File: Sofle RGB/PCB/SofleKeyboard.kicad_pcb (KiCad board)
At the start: 2 copper layers, 137.2 x 109.2 mm, 95 parts, among them J1 LED, J2 4PIN, J3 OLED, J4 key leds, J5 backlight sel, J6 indicator bypass, P1 i2c_pin, P2 i2c_pin, SW1 SW_PUSH-MX_W_LED, SW10 SW_PUSH-MX_W_LED, SW11 SW_PUSH-MX_W_LED, SW12 SW_PUSH-MX_W_LED, SW13 SW_PUSH-MX_W_LED, SW14 SW_PUSH-MX_W_LED, SW15 SW_PUSH-MX_W_LED, SW16 SW_PUSH-MX_W_LED, SW17 SW_PUSH-MX_W_LED, SW18 SW_PUSH-MX_W_LED, SW19 SW_PUSH-MX_W_LED, SW2 SW_PUSH-MX_W_LED, SW20 SW_PUSH-MX_W_LED, SW21 SW_PUSH-MX_W_LED, SW22 SW_PUSH-MX_W_LED, SW23 SW_PUSH-MX_W_LED, SW24 SW_PUSH-MX_W_LED, SW25 Rotary_Encoder_Switch, SW26 SW_PUSH-MX_W_LED, SW27 SW_PUSH-MX_W_LED, SW28 SW_PUSH-MX_W_LED, SW29 SW_PUSH-MX_W_LED, SW3 SW_PUSH-MX_W_LED, SW30 SW_PUSH-MX_W_LED, SW4 SW_PUSH-MX_W_LED, SW5 SW_PUSH-MX_W_LED, SW6 SW_PUSH-MX_W_LED, SW7 SW_PUSH-MX_W_LED, SW8 SW_PUSH-MX_W_LED, SW9 SW_PUSH-MX_W_LED, U1 ProMicro

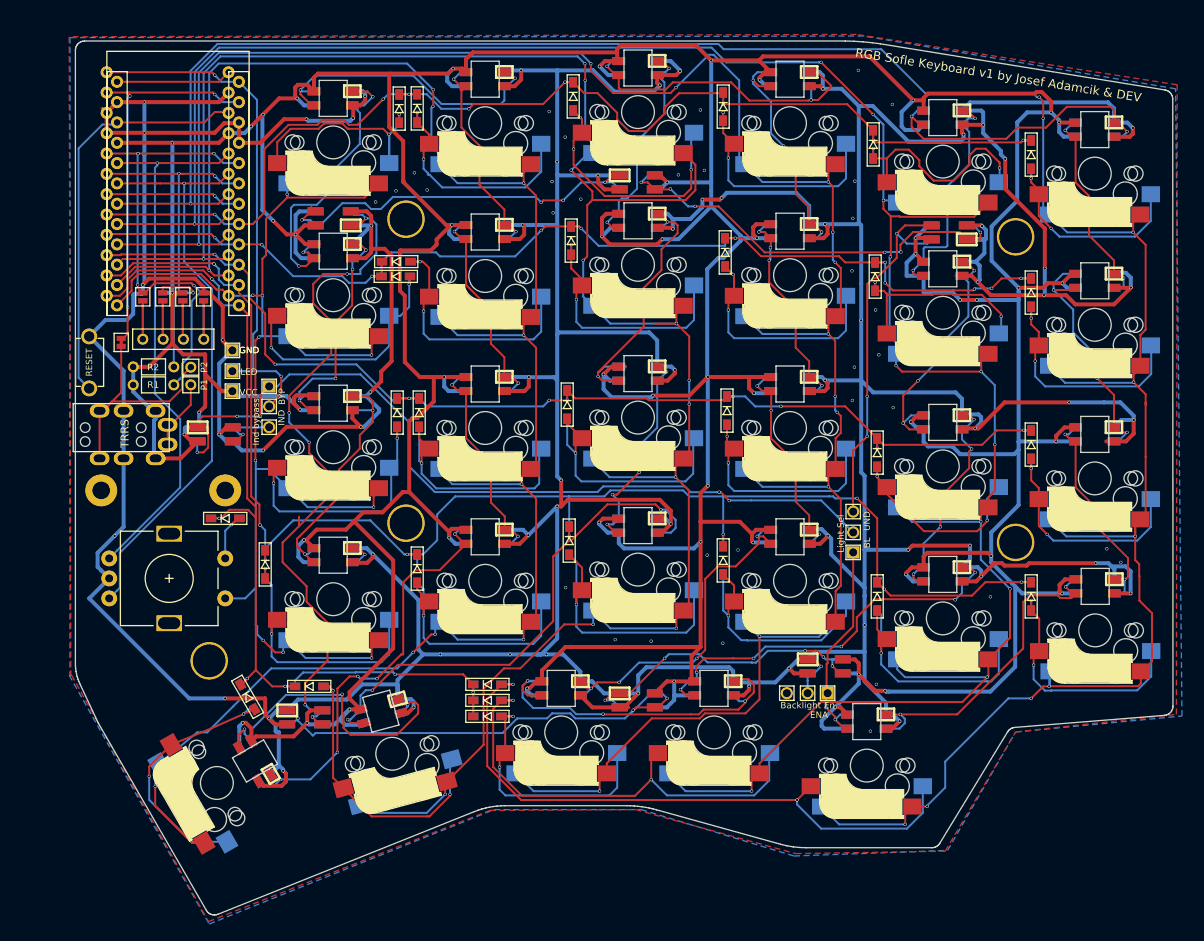
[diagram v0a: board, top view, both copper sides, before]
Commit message: added placement changes from r2, routed need to make any other changes, do pcb plates, and fix up the folders for mergeing
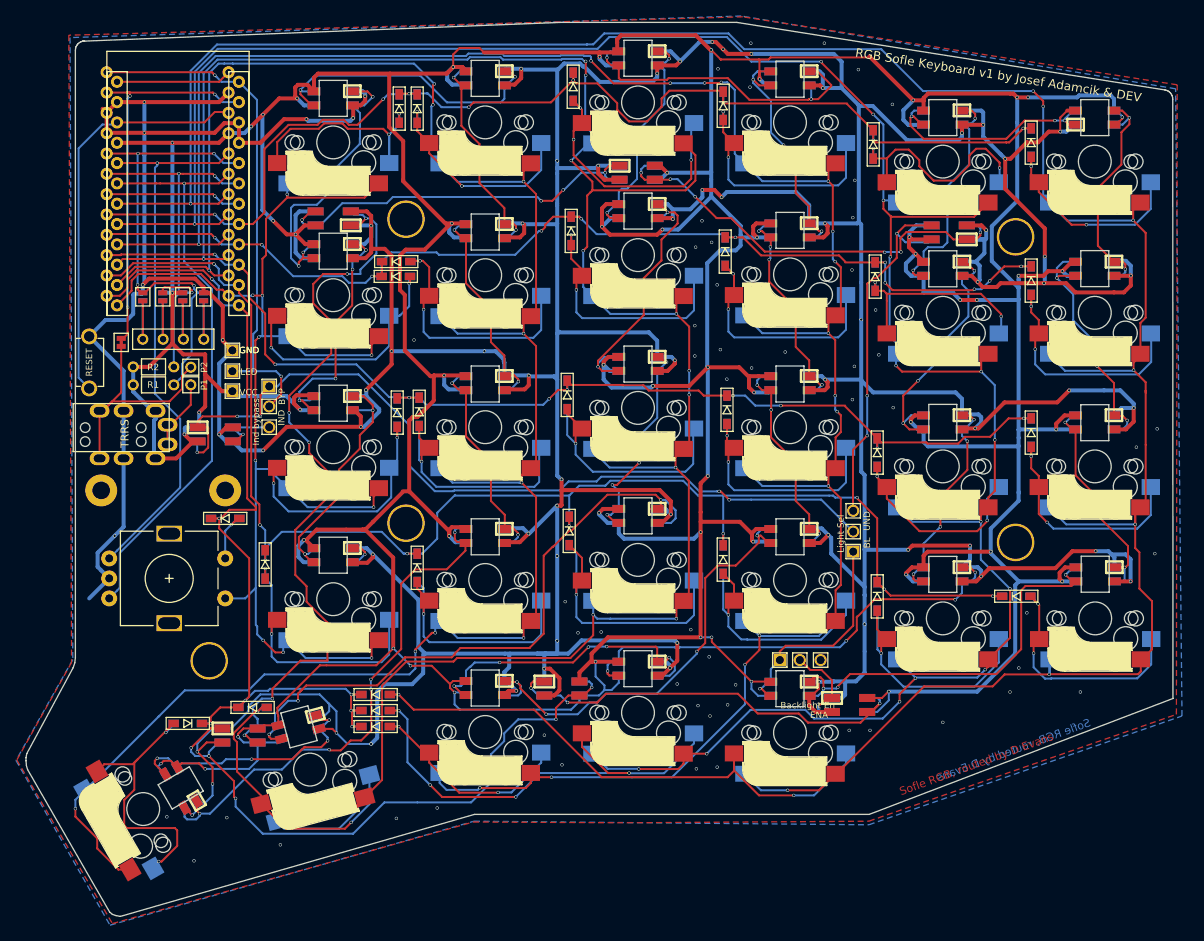
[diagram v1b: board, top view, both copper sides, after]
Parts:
- SW6: moved to B.Cu
- moved D28 14.0 mm to (125.8, 123.0)
- moved D29 14.0 mm to (125.8, 121.0)
- moved D30 14.0 mm to (125.8, 119.0)
- moved SW27 10.5 mm to (117.6, 128.4)
- moved SW30 10.4 mm to (177.6, 123.8)
- moved SW26 9.83 mm to (96.7, 133.4)
- moved SW29 9.81 mm to (158.6, 121.3)
- moved D35 9.53 mm to (149.1, 118.3)
- moved SW28 9.50 mm to (139.5, 123.7)
- moved D34 8.41 mm to (108.8, 124.1)
- moved D26 8.18 mm to (102.3, 122.6), turned to 180 degrees
- moved D27 7.55 mm to (110.4, 120.6)
- moved J5 7.27 mm to (176.3, 114.7), turned to 90 degrees
- moved D36 5.70 mm to (185.1, 120.3)
- moved D24 1.87 mm to (205.9, 106.7), turned to 0 degrees
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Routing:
- net VCC: track 911.1 -> 938.6 mm, vias 52 -> 56
- net Net-(D34-Pad1): track 59.0 -> 77.3 mm, vias 3 -> 5
- net Net-(SW22-Pad3): track 42.2 -> 56.5 mm
- net Net-(D35-Pad1): track 40.1 -> 53.7 mm, vias 5 -> 3
- net col4: track 245.1 -> 258.7 mm
- net Net-(SW21-Pad1): track 66.6 -> 79.9 mm
- net Net-(SW20-Pad3): track 53.9 -> 66.2 mm
- net col3: track 267.0 -> 276.7 mm
- net Net-(SW28-Pad3): track 47.7 -> 38.0 mm, vias 3 -> 5
- net Net-(SW24-Pad3): track 41.0 -> 50.3 mm, vias 2 -> 3
- net Net-(SW5-Pad3): track 39.6 -> 31.1 mm, vias 2 -> 3
- net Net-(SW26-Pad3): track 39.6 -> 31.5 mm, vias 3 -> 4
- net row3: track 191.0 -> 183.2 mm
- net Net-(SW23-Pad1): track 51.1 -> 58.4 mm, vias 6 -> 4
- net Net-(D30-Pad2): track 78.4 -> 71.2 mm
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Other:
- board size 137.2 x 109.2 mm -> 143.4 x 111.8 mm
- board text added: "Sofle RGB, routed by D Evans"

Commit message: release version of the sofle rgb, routing done, case made, there are some slight oddities in the spacing of some keys, but they are very small
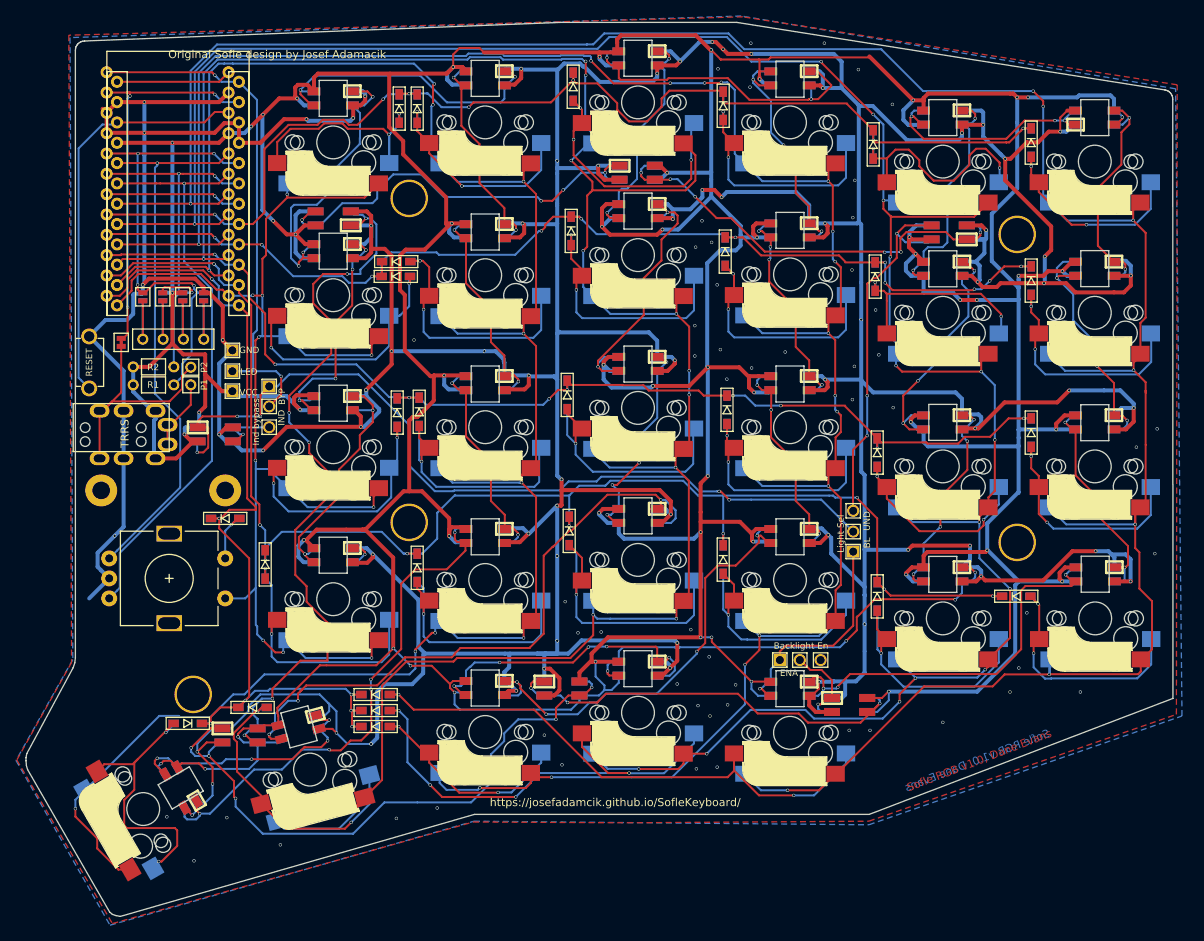
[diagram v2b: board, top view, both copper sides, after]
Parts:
- added G***: LOGO, dane:gecko-logo, B.Cu at (201.0, 122.8)
- added G***: LOGO, dane:gecko-logo, F.Cu at (200.2, 122.8)
- moved TH7 4.65 mm to (103.0, 119.0)
- moved TH3 2.55 mm to (130.0, 57.1)
- moved TH5 0.43 mm to (130.0, 97.6)
- moved TH4 0.43 mm to (206.2, 61.8)
- moved TH6 0.38 mm to (206.2, 100.0)
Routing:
- net Net-(D31-Pad3): track 48.5 -> 51.4 mm
- net GND: track 988.5 -> 989.6 mm
- net VCC: track 938.6 -> 939.7 mm
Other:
- board text added: "Original Sofle design by Josef Adamacik"
- board text added: "Sofle RGB v1.0, Dane Evans"
- board text added: "https://josefadamcik.github.io/SofleKeyboard/"
- board text removed: "RGB Sofle Keyboard v1 by Josef Adamcik & DEV"
- board text removed: "Sofle RGB, routed by D Evans"
